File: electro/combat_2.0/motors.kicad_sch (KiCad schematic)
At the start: 9 parts

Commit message: 20A Current sensor
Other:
- moved on the sheet: C?, J?, U?

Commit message: PCB V0
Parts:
- C3, C4, C5, C6, C7, C8: renamed from C?; footprint (none) -> Capacitor_SMD:C_0805_2012Metric
- J2, J3: renamed from J?; footprint (none) -> TerminalBlock:TerminalBlock_Altech_AK300-2_P5.00mm
- gave numbers to parts that had none: 1
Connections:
- net at C6.1, U3.1 (AO1), U3.2 (AO1): now also J2.2 (Pin_2); no longer J2.1 (Pin_1)
- net at C6.2, U3.5 (AO2), U3.6 (AO2): now also J2.1 (Pin_1); no longer J2.2 (Pin_2)
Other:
- moved on the sheet: J2, J3

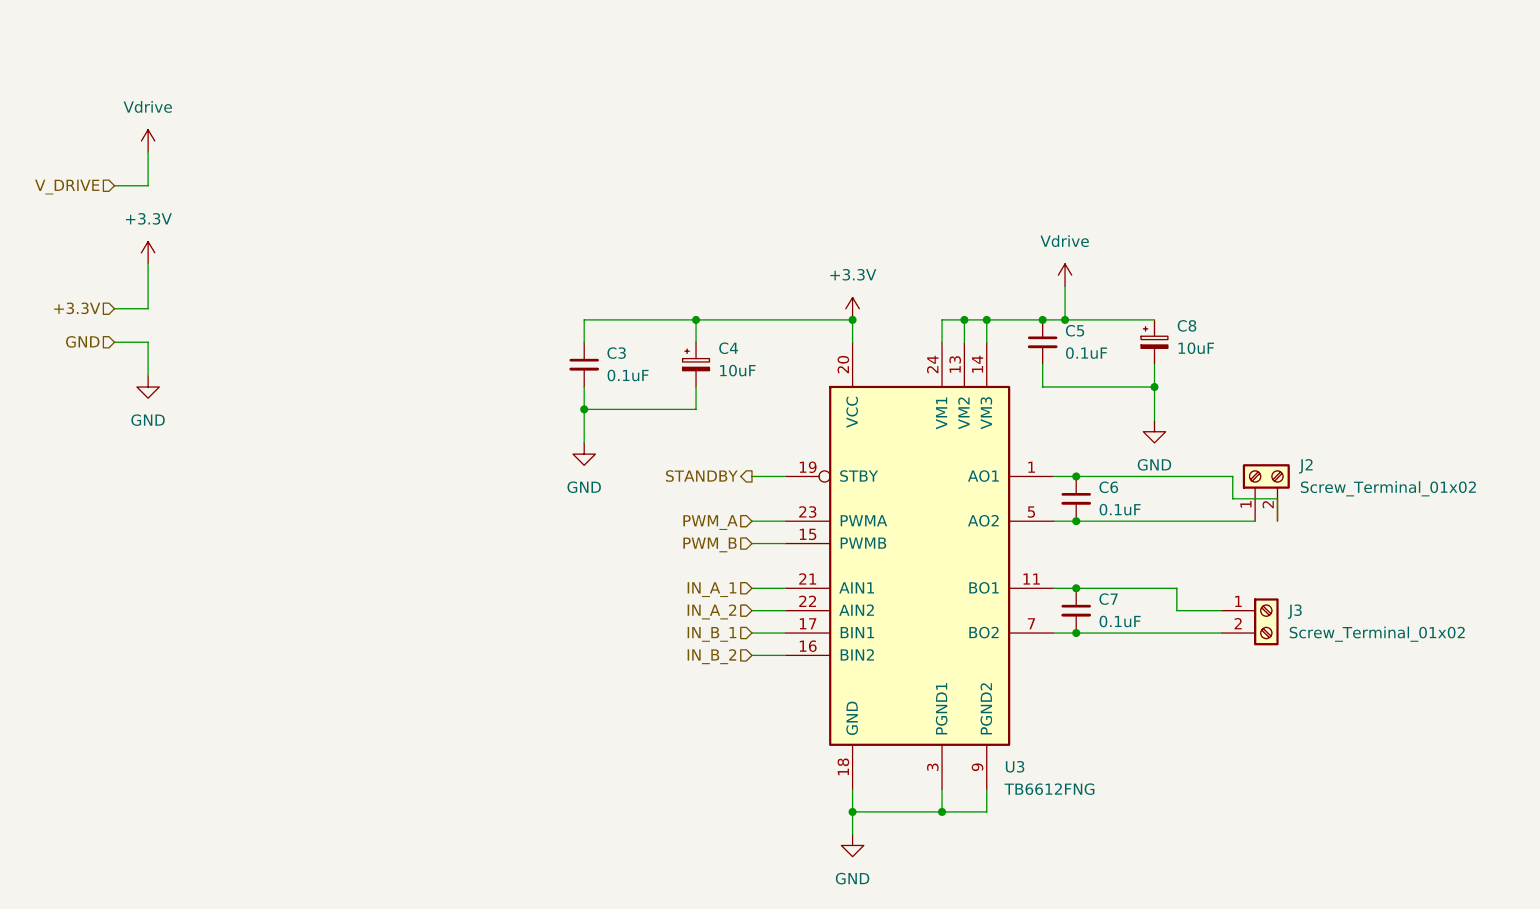
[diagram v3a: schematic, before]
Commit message: Standarized schematic labels
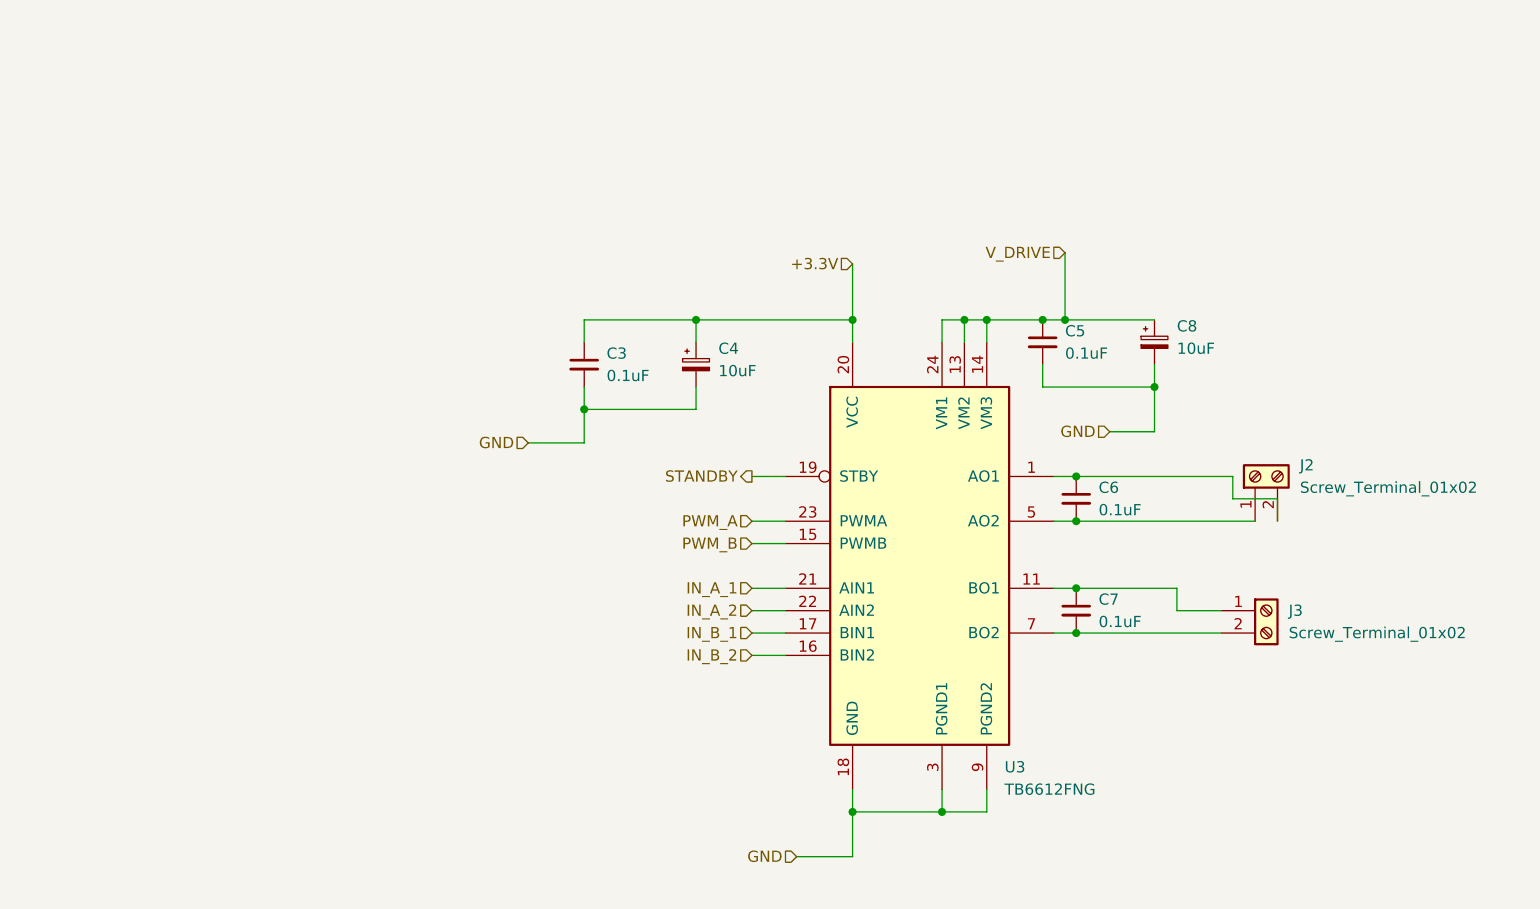
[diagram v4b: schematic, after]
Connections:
- net Vdrive renamed V_DRIVE

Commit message: Changed MCU to ESP32-DEVKITC, cleared some ERC errors
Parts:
- C4, C8: footprint Capacitor_SMD:C_0805_2012Metric -> Capacitor_SMD:CP_Elec_4x5.4
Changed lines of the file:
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@@
       (effects (font (size 1.27 1.27)) (justify left))
     )
-    (property "Footprint" "Capacitor_SMD:C_0805_2012Metric" (at 128.27 63.5 0)
+    (property "Footprint" "Capacitor_SMD:CP_Elec_4x5.4" (at 128.27 63.5 0)
       (effects (font (size 1.27 1.27)) hide)
     )
@@
       (effects (font (size 1.27 1.27)) (justify left))
     )
-    (property "Footprint" "Capacitor_SMD:C_0805_2012Metric" (at 180.34 60.96 0)
+    (property "Footprint" "Capacitor_SMD:CP_Elec_4x5.4" (at 180.34 60.96 0)
       (effects (font (size 1.27 1.27)) hide)
     )

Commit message: Updated some footprints
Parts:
- C3, C5, C6, C7: footprint Capacitor_SMD:C_0805_2012Metric -> Capacitor_SMD:C_1206_3216Metric_Pad1.33x1.80mm_HandSolder
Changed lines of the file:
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@@
       (effects (font (size 1.27 1.27)) (justify left))
     )
-    (property "Footprint" "Capacitor_SMD:C_0805_2012Metric" (at 167.64 60.96 0)
+    (property "Footprint" "Capacitor_SMD:C_1206_3216Metric_Pad1.33x1.80mm_HandSolder" (at 167.64 60.96 0)
       (effects (font (size 1.27 1.27)) hide)
     )
@@
       (effects (font (size 1.27 1.27)) (justify left))
     )
-    (property "Footprint" "Capacitor_SMD:C_0805_2012Metric" (at 115.57 63.5 0)
+    (property "Footprint" "Capacitor_SMD:C_1206_3216Metric_Pad1.33x1.80mm_HandSolder" (at 115.57 63.5 0)
       (effects (font (size 1.27 1.27)) hide)
     )
@@
       (effects (font (size 1.27 1.27)) (justify left))
     )
-    (property "Footprint" "Capacitor_SMD:C_0805_2012Metric" (at 171.45 91.44 0)
+    (property "Footprint" "Capacitor_SMD:C_1206_3216Metric_Pad1.33x1.80mm_HandSolder" (at 171.45 91.44 0)
       (effects (font (size 1.27 1.27)) hide)
     )
@@
       (effects (font (size 1.27 1.27)) (justify left))
     )
-    (property "Footprint" "Capacitor_SMD:C_0805_2012Metric" (at 171.45 78.74 0)
+    (property "Footprint" "Capacitor_SMD:C_1206_3216Metric_Pad1.33x1.80mm_HandSolder" (at 171.45 78.74 0)
       (effects (font (size 1.27 1.27)) hide)
     )

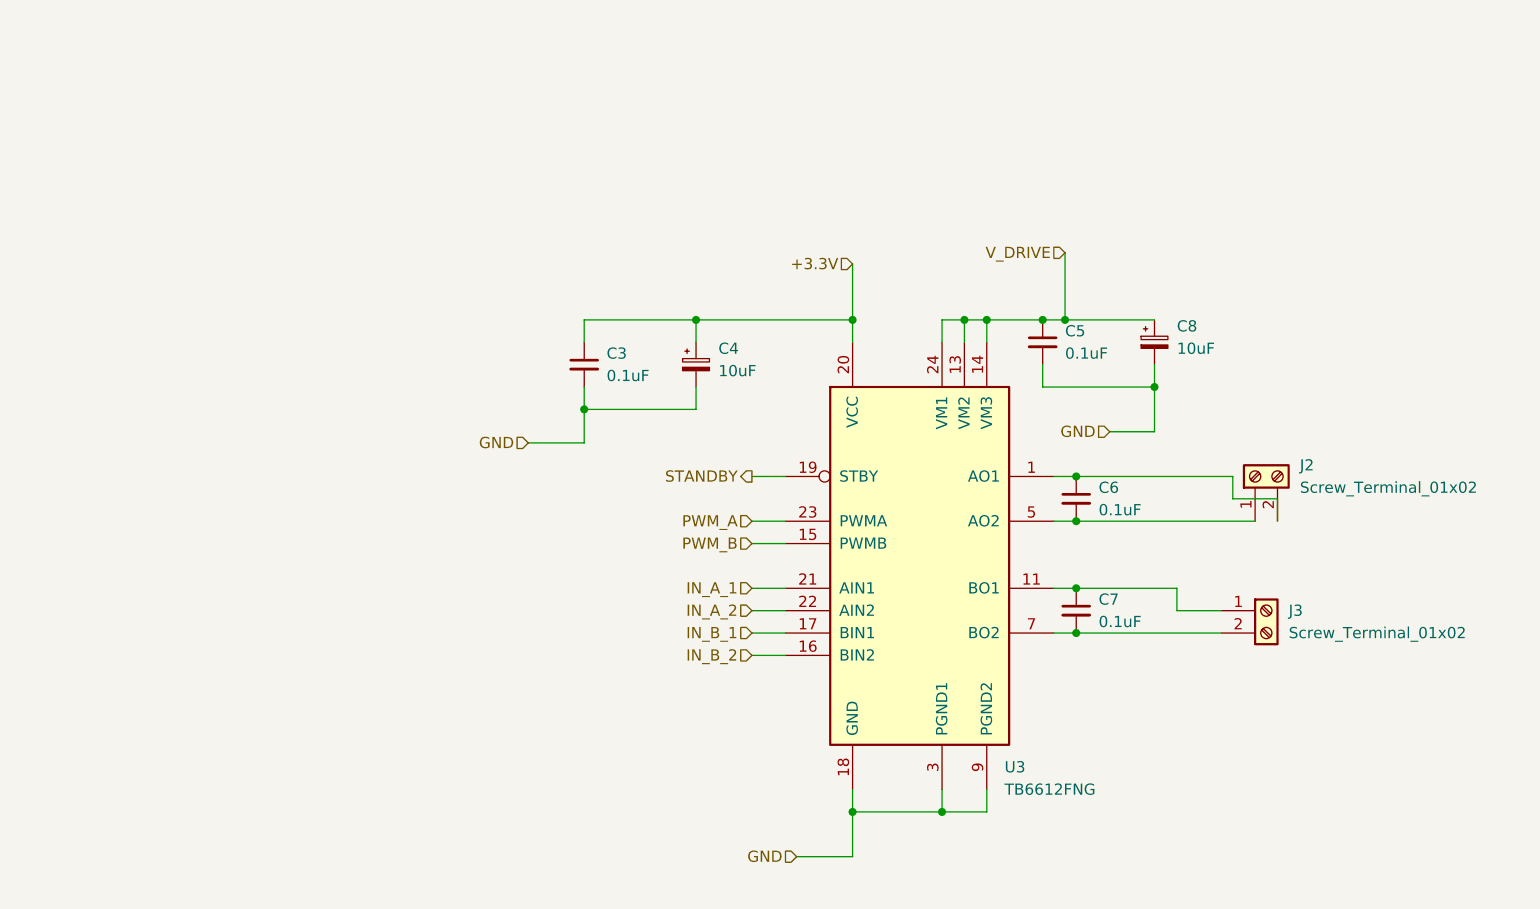
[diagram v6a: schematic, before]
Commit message: Changed Devkit for ESP32-WROOM device. Added LDO, some other peripherals
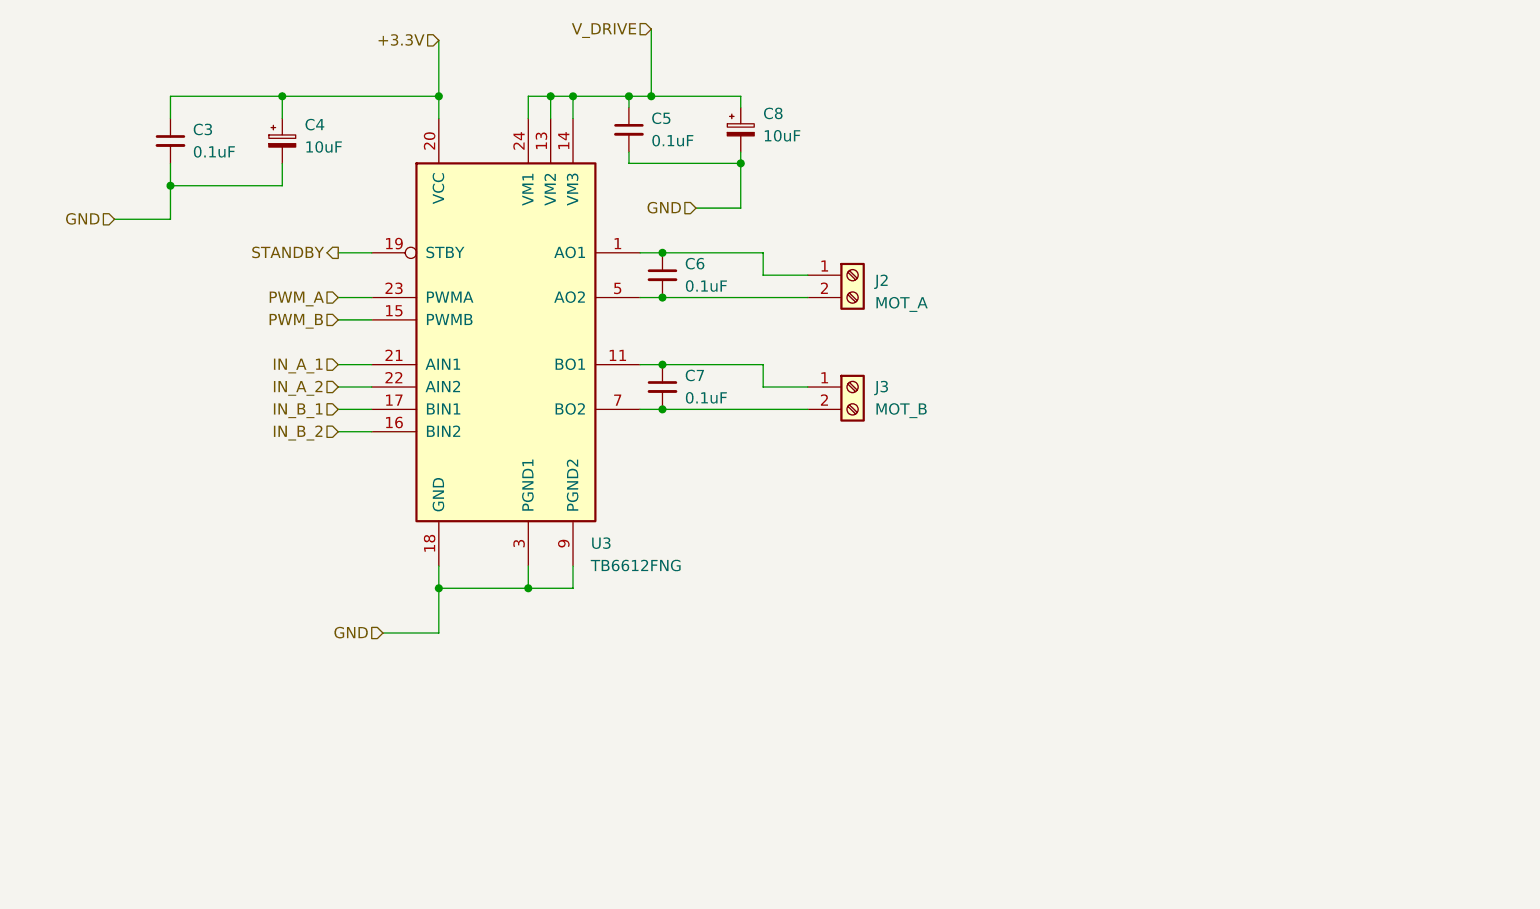
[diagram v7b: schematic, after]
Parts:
- J2: value Screw_Terminal_01x02 -> MOT_A
- J3: value Screw_Terminal_01x02 -> MOT_B
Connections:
- net at C6.1, U3.1 (AO1), U3.2 (AO1): now also J2.1 (Pin_1); no longer J2.2 (Pin_2)
- net at C6.2, U3.5 (AO2), U3.6 (AO2): now also J2.2 (Pin_2); no longer J2.1 (Pin_1)
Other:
- moved on the sheet: C3, C4, C5, C6, C7, C8, J2, J3, U3
